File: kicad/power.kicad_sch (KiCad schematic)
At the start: 3 parts, among them U201 NCP1117-3.3_SOT223

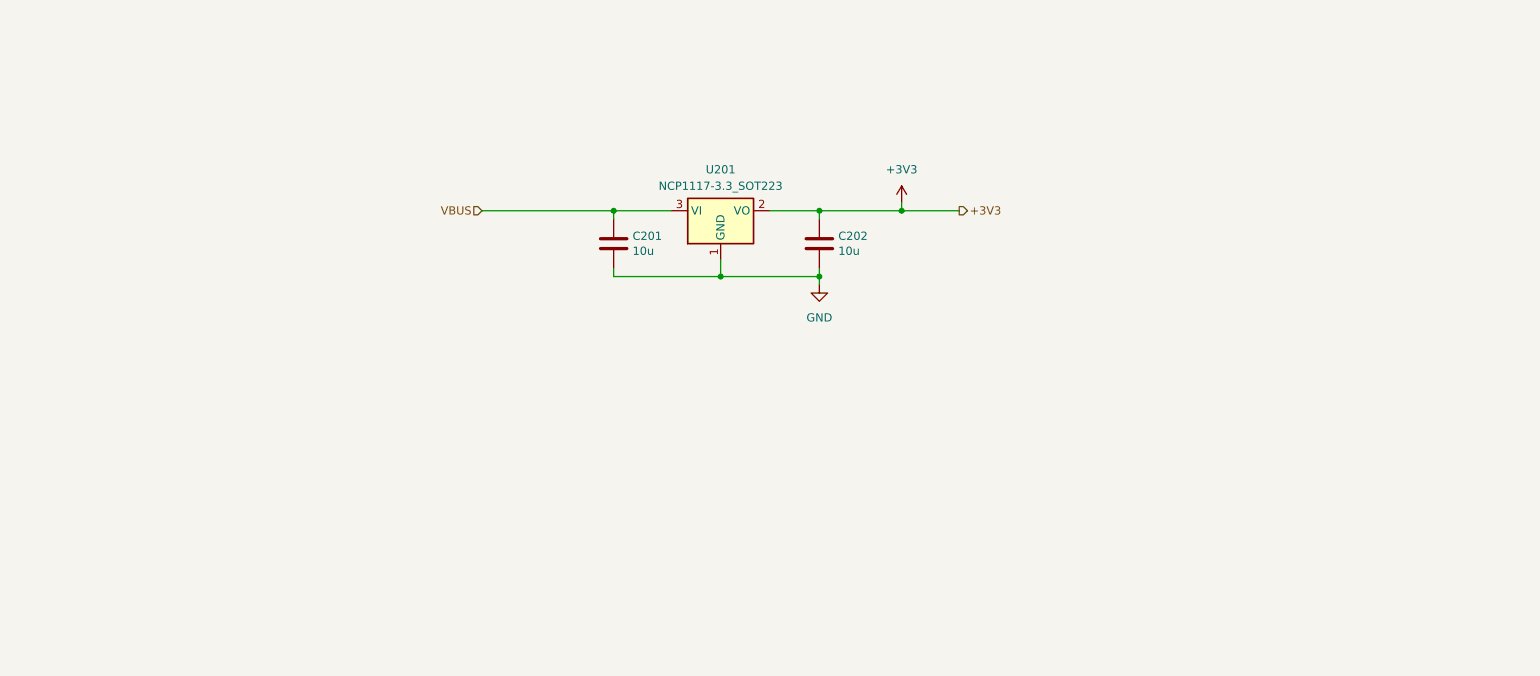
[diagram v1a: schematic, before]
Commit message: changed from rp2040 to nrf
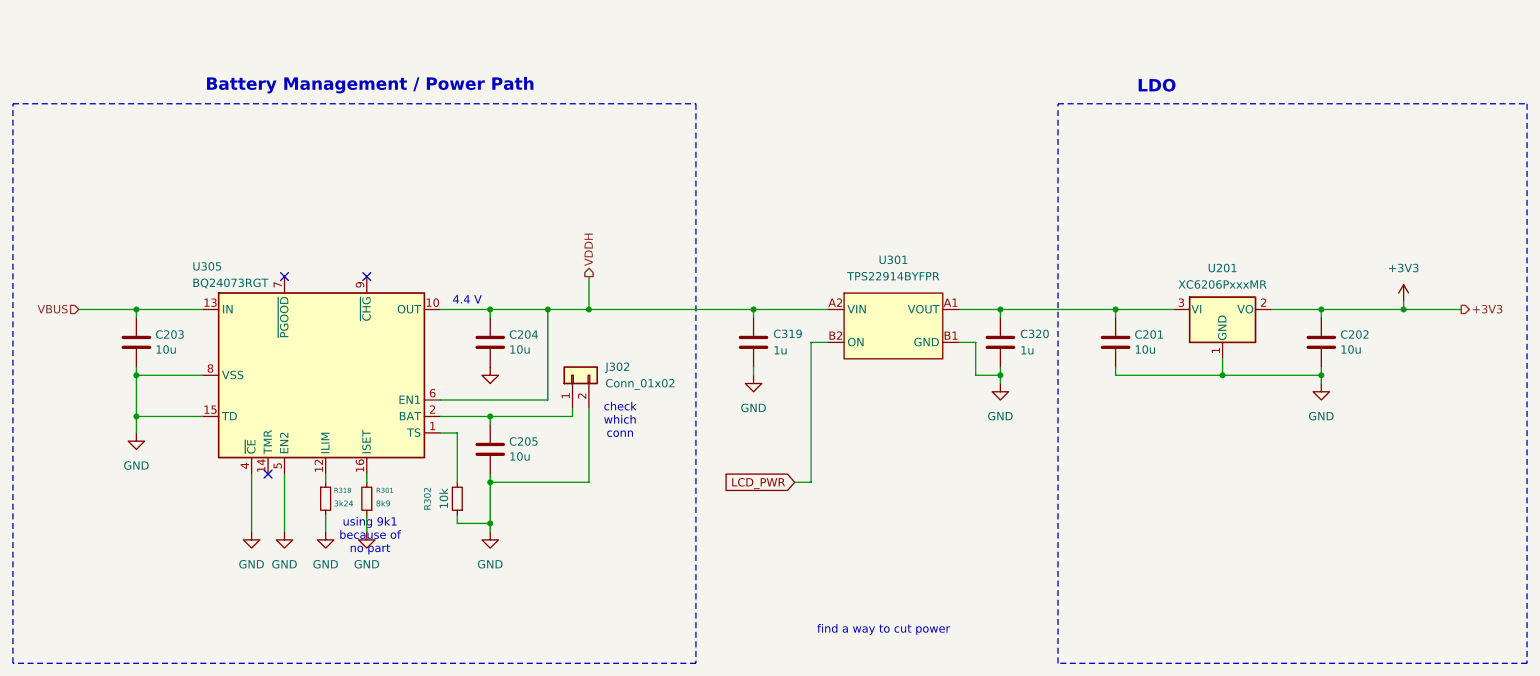
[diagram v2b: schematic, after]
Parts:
- removed U201: NCP1117-3.3_SOT223, Package_TO_SOT_SMD:SOT-223, symbol Regulator_Linear:NCP1117-3.3_SOT223
- added C203, C204, C205: 10u, Capacitor_SMD:C_0402_1005Metric, symbol Device:C
- added C319, C320: 1u, Capacitor_SMD:C_0402_1005Metric, symbol Device:C
- added J302: Conn_01x02, Connector_JST:JST_PH_S2B-PH-K_1x02_P2.00mm_Horizontal, symbol Connector_Generic:Conn_01x02
- added R301: 8k9, Resistor_SMD:R_0402_1005Metric, symbol Device:R_Small
- added R302: 10k, Resistor_SMD:R_0402_1005Metric, symbol Device:R_Small
- added R318: 3k24, Resistor_SMD:R_0402_1005Metric, symbol Device:R_Small
- added U201: XC6206PxxxMR, Package_TO_SOT_SMD:SOT-23-3, symbol Regulator_Linear:XC6206PxxxMR
- added U301: TPS22914BYFPR, Package_BGA:Texas_PicoStar_BGA-4_0.758x0.758mm_Layout2x2_P0.4mm, symbol Pocketboard:TPS22914BYFPR
- added U305: BQ24073RGT, Package_DFN_QFN:VQFN-16-1EP_3x3mm_P0.5mm_EP1.6x1.6mm, symbol Pocketboard:BQ24073RGT
- C201, C202: footprint Capacitor_SMD:C_0603_1608Metric -> Capacitor_SMD:C_0402_1005Metric; JLCPCB Part # C19702 -> C15525
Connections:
- net +3V3: now also U201.2 (VO)
- net GND: now also C203.2, C204.2, C205.2, C319.2, C320.2, J302.2 (Pin_2), R301.1, R302.1, R318.2, U201.1 (GND), U301.B1 (GND), U305.15 (TD), U305.17 (VSS), U305.4 (~{CE}), U305.5 (EN2), U305.8 (VSS)
- net VBUS: now also C203.1, U305.13 (IN); no longer C201.1
- new net: C201.1, C320.1, U201.3 (VI), U301.A1 (VOUT)
- new net: R301.2, U305.16 (ISET)
- new net: R302.2, U305.1 (TS)
- new net: R318.1, U305.12 (ILIM)
- new net: C205.1, J302.1 (Pin_1), U305.2 (BAT), U305.3 (BAT)
- new net LCD_PWR: U301.B2 (ON)
- new net VDDH: C204.1, C319.1, U301.A2 (VIN), U305.10 (OUT), U305.11 (OUT), U305.6 (EN1)
- no-connect marks 0 -> 3
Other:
- note added: "4.4 V"
- note added: "Battery Management / Power Path"
- note added: "LDO"
- note added: "check which conn"
- note added: "find a way to cut power"
- note added: "using 9k1 because of no part"
- moved on the sheet: C201, C202

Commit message: board routed
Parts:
- added C321: 100n, Capacitor_SMD:C_0402_1005Metric, symbol Device:C
- added JP301: Jumper_2_Open, Jumper:SolderJumper-2_P1.3mm_Open_RoundedPad1.0x1.5mm, symbol Jumper:Jumper_2_Open
- added R303: 10k, Resistor_SMD:R_0402_1005Metric, symbol Device:R_Small
- added SW301: SW_SPST, Button_Switch_SMD:SW_SPDT_PCM12, symbol Switch:SW_SPST
- added U302: MAX17048, Pocketboard:21-0555B_W80B1-1_MXM, symbol MAX17048:MAX17048
- J302: footprint Connector_JST:JST_PH_S2B-PH-K_1x02_P2.00mm_Horizontal -> Connector_PinSocket_2.54mm:PinSocket_1x02_P2.54mm_Vertical
- R301: value 8k9 -> 10k; JLCPCB Part # C25926 -> C25531
- U201: JLCPCB Part # (none) -> C5446
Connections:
- net GND: now also C321.2, R303.1, U302.A1 (CTG), U302.A4 (GND), U302.B3 (QSTRT)
- net VDDH: now also C201.1, C320.1, U201.3 (VI), U301.A1 (VOUT); no longer C204.1, C319.1, U301.A2 (VIN), U305.10 (OUT), U305.11 (OUT), U305.6 (EN1)
- net VBAT: now reaches C205.1, J302.1 (Pin_1), U305.2 (BAT), U305.3 (BAT)
- net VBAT: now also C321.1, U302.A2 (CELL), U302.A3 (VDD)
- net LCD_PWR: no longer names the net of U301.B2 (ON)
- net LCD_PWR: now also JP301.1 (A), R303.2, SW301.2 (B)
- new net: C204.1, C319.1, JP301.2 (B), SW301.1 (A), U301.A2 (VIN), U305.10 (OUT), U305.11 (OUT), U305.6 (EN1)
- new net BAT_I2C_SCL: U302.B2 (SCL)
- new net BAT_I2C_SDA: U302.B1 (SDA)
- no-connect marks 3 -> 4
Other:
- note added: "note: use internal pullups for these"
- note removed: "using 9k1 because of no part"
- moved on the sheet: C319
